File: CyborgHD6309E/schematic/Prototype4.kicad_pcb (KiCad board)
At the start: 2 copper layers, 95 x 72 mm, 25 parts, among them J1 Conn_AVR_UPDI, J2 Conn_AVR_UPDI, SW1 TSD1265, U1 ATmega4809-P, U2 HM628128DLP-5, U3 HD63C09E, U4 ATtiny412-SS, U5 CD74HCT30, U6 CD74HCT688

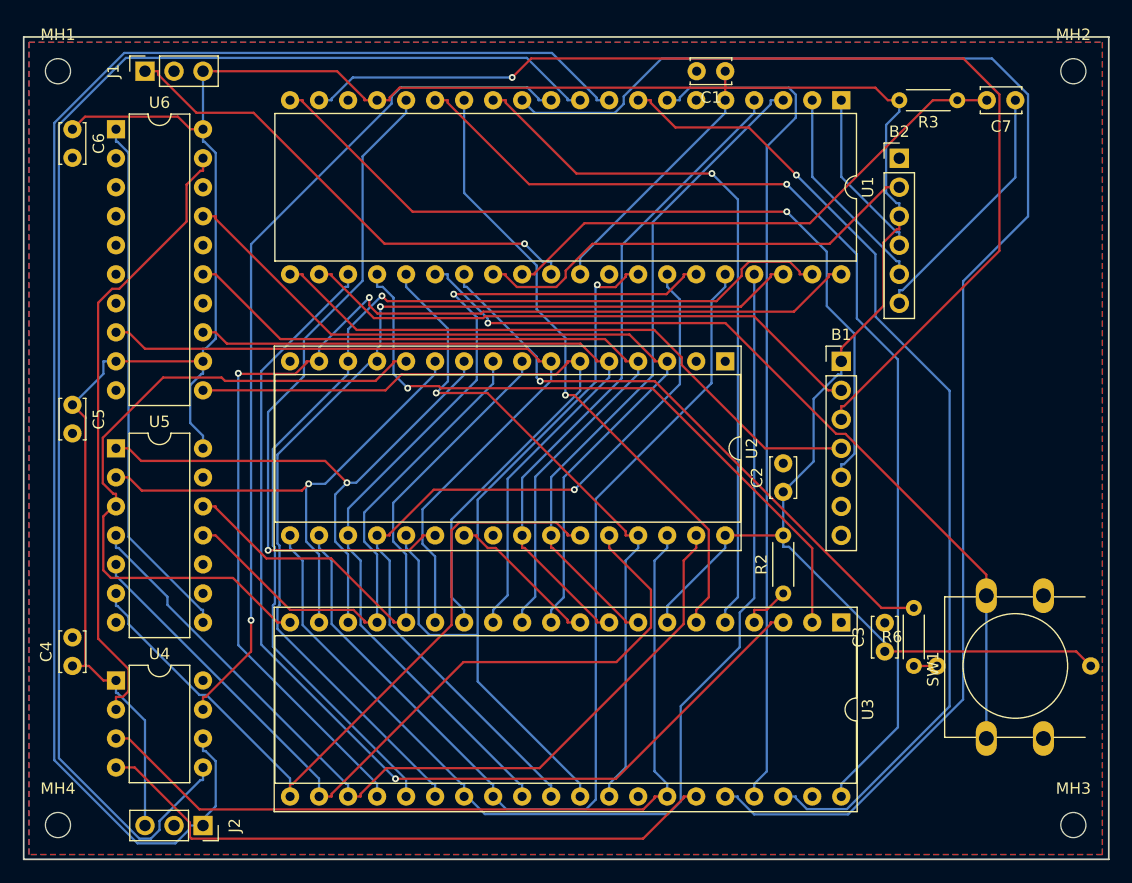
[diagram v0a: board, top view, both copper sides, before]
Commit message: [CyborgHD6309E] Update pins map
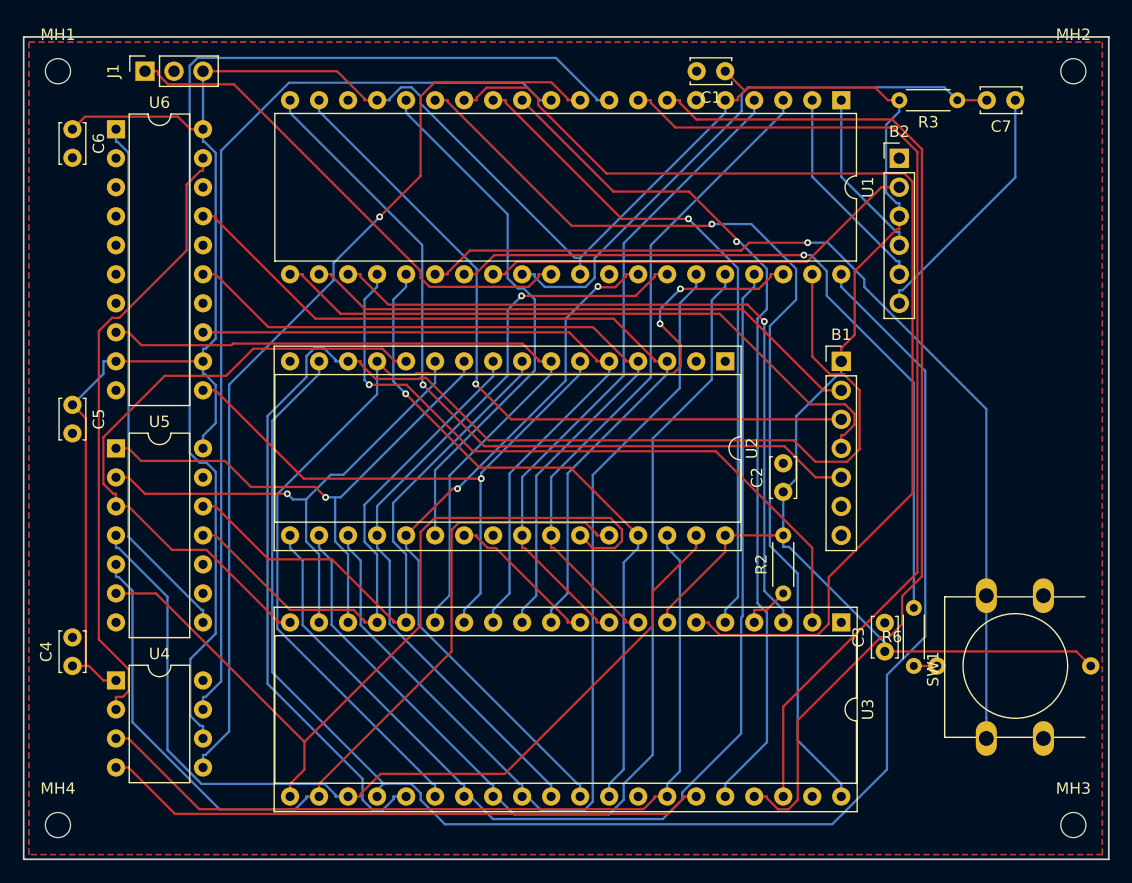
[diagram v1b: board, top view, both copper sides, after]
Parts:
- removed J2: Conn_AVR_UPDI, Connector_PinSocket_2.54mm:PinSocket_1x03_P2.54mm_Vertical
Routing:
- net /AVMA: track 129.4 -> 76.1 mm, vias 0 -> 1
- net /BA: track 55.5 -> 97.9 mm, vias 1 -> 0
- net /~STEP~: track 124.4 -> 82.0 mm, vias 0 -> 1
- net /D7: track 101.0 -> 139.7 mm, vias 2 -> 0
- net /~ACK~: track 134.5 -> 100.3 mm
- net /SD_DI: track 96.8 -> 64.0 mm
- net /D6: track 93.0 -> 119.8 mm, vias 1 -> 0
- net /~IRQ~: track 92.0 -> 65.3 mm
- net VCC: track 280.0 -> 260.5 mm
- net /~RESET~: track 75.1 -> 90.8 mm
- net /~RAM_E~: track 59.7 -> 46.7 mm, vias 1 -> 0
- net /~USR_LED~: track 53.2 -> 65.8 mm
- net /~USR_SW~: track 73.9 -> 84.8 mm
- net /D0: track 70.9 -> 62.5 mm, vias 1 -> 2
- net /D2: track 78.0 -> 86.4 mm, vias 1 -> 0
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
